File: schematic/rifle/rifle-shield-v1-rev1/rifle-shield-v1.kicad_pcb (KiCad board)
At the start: 2 copper layers, 43 parts, among them K1 Display2, K3 VCC, P1 Power, P10 MCU2, P11 RFID-RC522-MODULE, P12 NRF24L01, P13 IR_LED, P15 Vibro&flash, P2 MCU1, P3 Mag&fireMode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

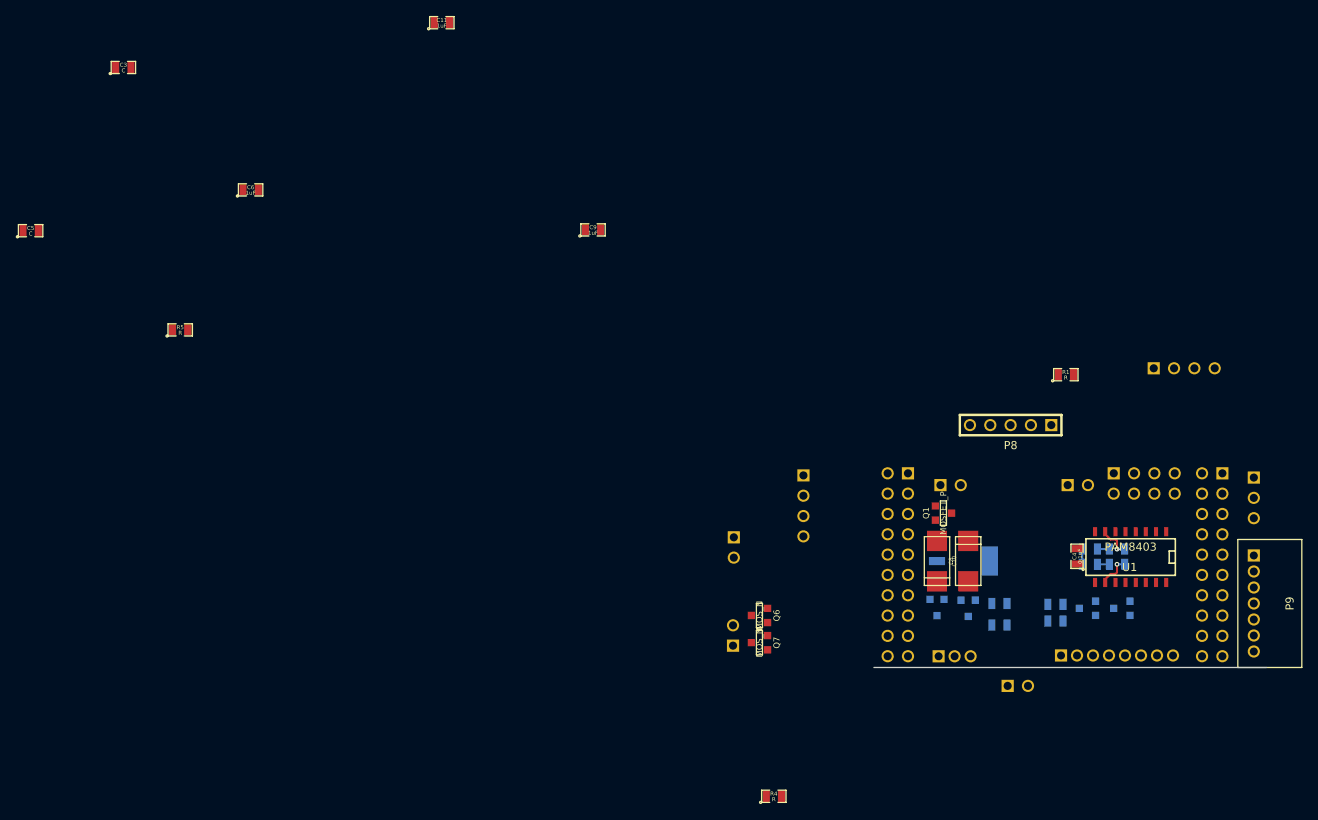
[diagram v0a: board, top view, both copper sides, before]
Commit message: Rifle shield without display done
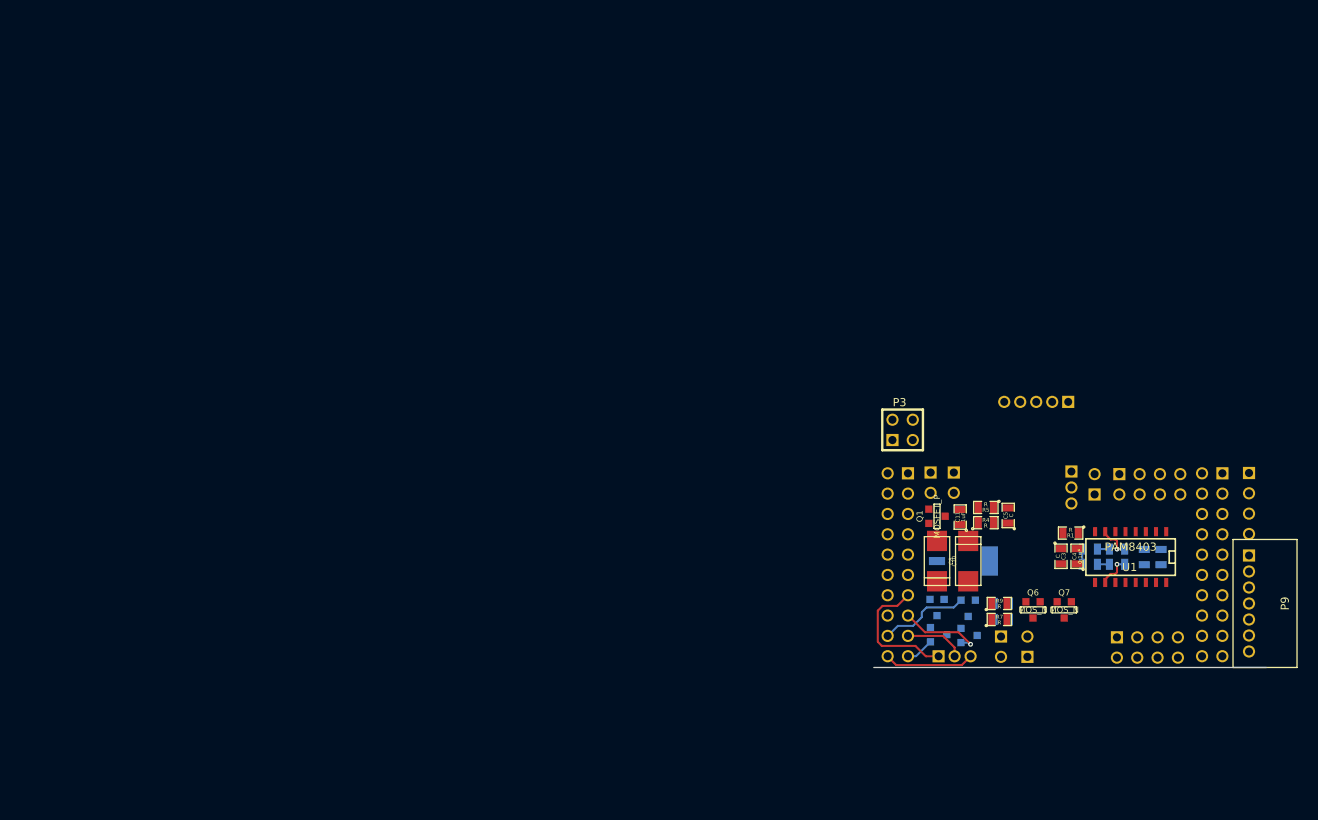
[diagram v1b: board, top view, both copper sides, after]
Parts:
- C6, C9: moved to B.Cu
- K3: footprint PIN_ARRAY_3X1 -> PIN_ARRAY-3X1-2mm-horiz
- P11: footprint PIN_ARRAY-8X1-2mm-horiz -> pin_array_4x2
- P3: footprint PIN_ARRAY_4x1 -> PIN_ARRAY_2X2; moved to F.Cu
- P8: footprint PIN_ARRAY_5x1 -> PIN_ARRAY-5X1-2mm-horiz; moved to B.Cu
- R7, R9: moved to F.Cu
- moved C3 132.2 mm to (85.9, 58.0), turned to 270 degrees
- moved C5 127.3 mm to (79.3, 52.9), turned to 90 degrees
- moved C6 122.7 mm to (98.4, 58.1), turned to 90 degrees
- moved R5 103.1 mm to (76.5, 51.9), turned to 180 degrees
- moved C11 89.5 mm to (73.3, 53.1), turned to 90 degrees
- moved C9 80.1 mm to (96.3, 58.1), turned to 90 degrees
- moved R4 43.3 mm to (76.5, 53.8)
- moved Q7 38.3 mm to (86.3, 64.7), turned to 0 degrees
- moved P15 36.8 mm to (81.7, 69.3)
- moved Q6 34.2 mm to (82.4, 64.7), turned to 0 degrees
- moved P7 28.7 mm to (72.5, 48.8)
- moved K3 22.8 mm to (87.2, 49.4)
- moved R1 19.8 mm to (87.1, 55.1), turned to 180 degrees
- moved Q3 19.4 mm to (74.4, 67.9), turned to 270 degrees
- moved Q5 18.9 mm to (70.6, 67.8), turned to 270 degrees
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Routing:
- net N-0000036: track 0.00 -> 16.8 mm
- net N-0000049: track 0.00 -> 11.4 mm
- net N-0000046: track 0.00 -> 11.3 mm
- net N-0000050: track 0.00 -> 10.6 mm, vias 0 -> 1
- net N-0000047: track 0.00 -> 7.53 mm
- net N-0000048: track 0.00 -> 3.56 mm
